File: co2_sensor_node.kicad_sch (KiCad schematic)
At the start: 6 parts, among them J1 Conn_01x05, J2 Conn_01x03

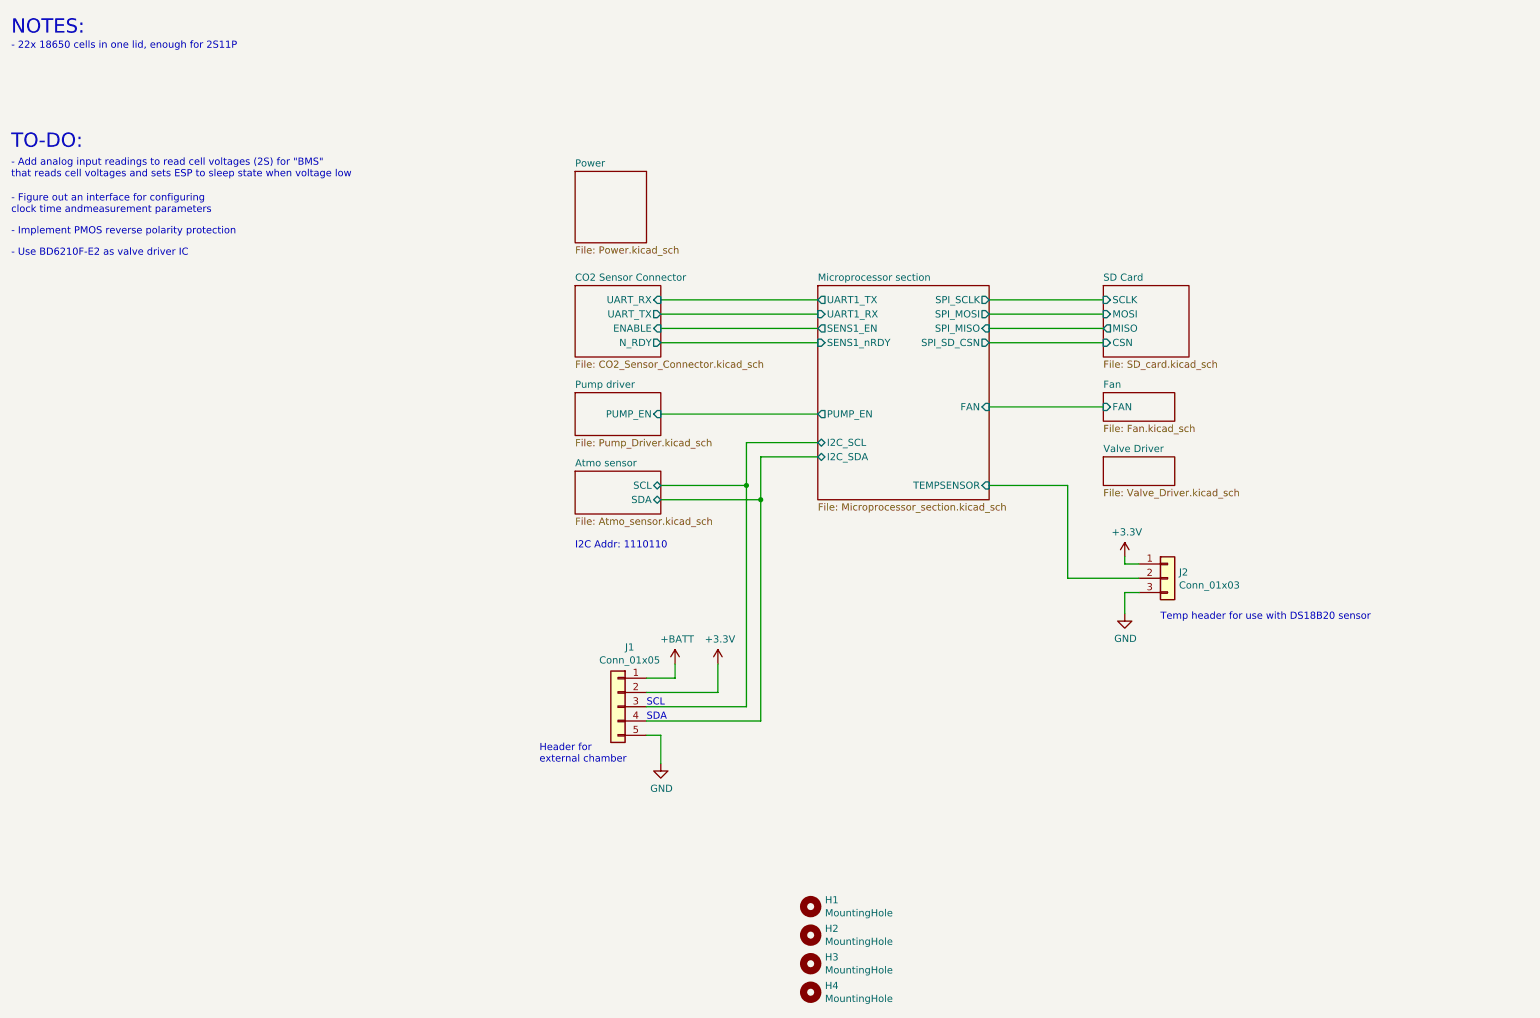
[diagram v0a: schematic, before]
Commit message: Move to KiCad v6, redesign circuit for chamber
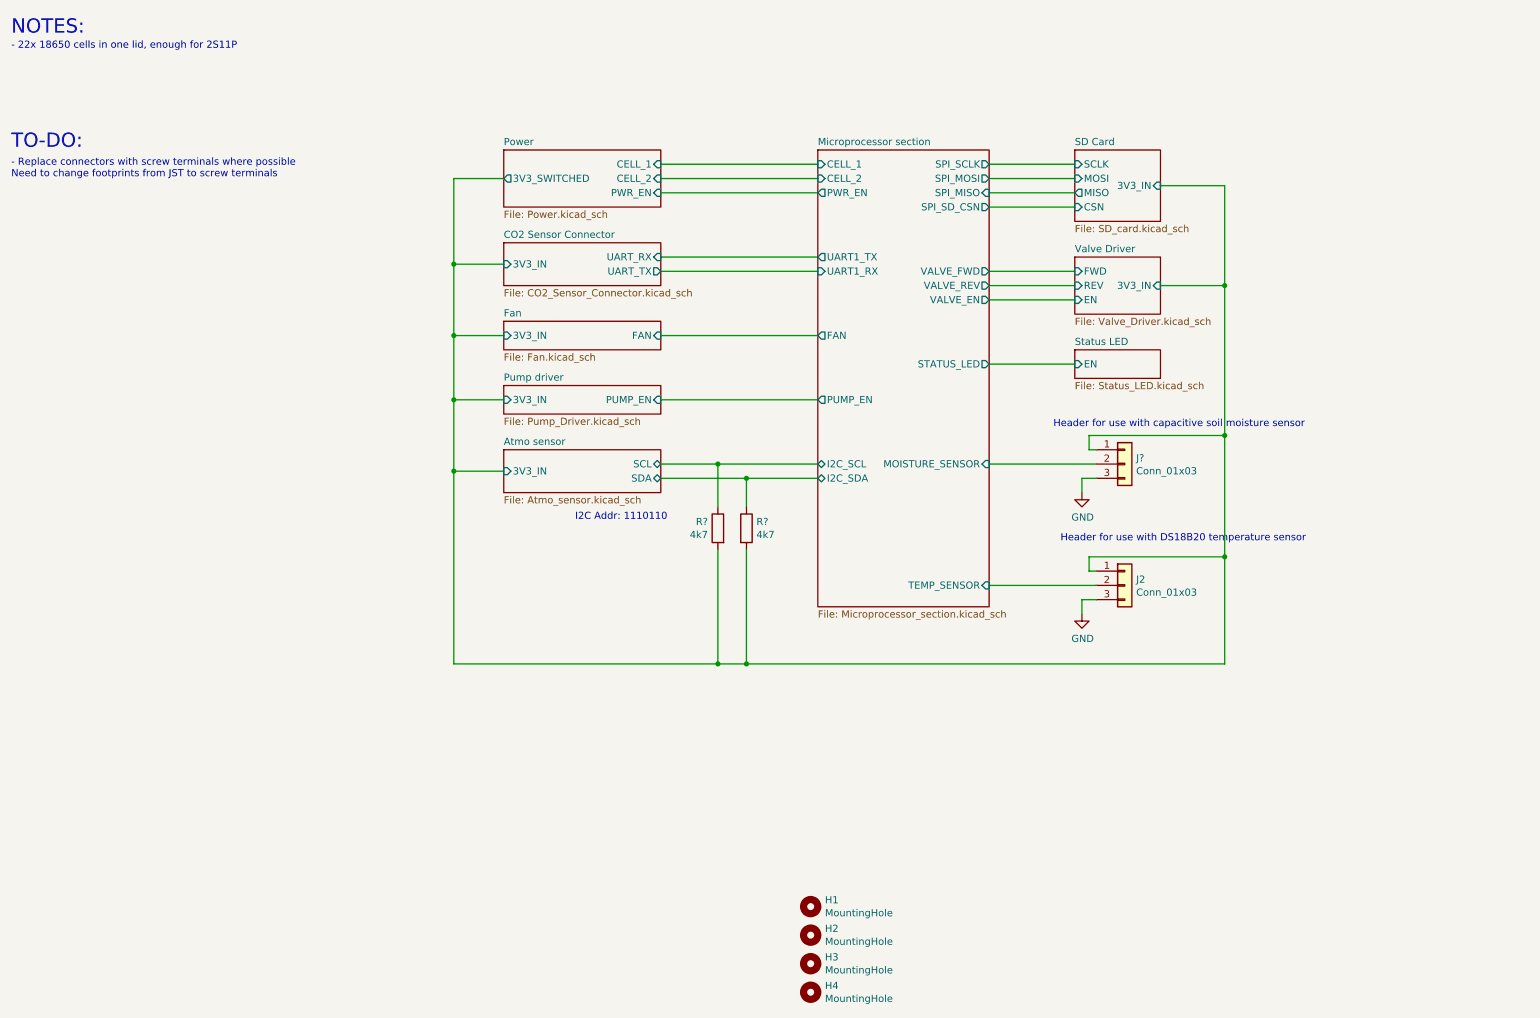
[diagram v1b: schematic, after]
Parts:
- removed J1: Conn_01x05, Connector_JST:JST_XH_B5B-XH-AM_1x05_P2.50mm_Vertical, symbol Connector_Generic:Conn_01x05
- added J?: Conn_01x03, Connector_JST:JST_XH_B3B-XH-AM_1x03_P2.50mm_Vertical, symbol Connector_Generic:Conn_01x03
- added R? (x2): 4k7, Resistor_SMD:R_0603_1608Metric, symbol Device:R
- J2: LCSC (none) -> C474882
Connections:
- net Atmo sensor/SCL: now also R?.1
- net Atmo sensor/SDA: now also R?.1
- net GND: now also J?.3 (Pin_3)
- net +3V3 renamed Atmo sensor/3V3_IN
- net Atmo sensor/3V3_IN: now also J?.1 (Pin_1), R?.2, R?.2
- net Microprocessor section/TEMPSENSOR renamed Microprocessor section/TEMP_SENSOR
- new net Microprocessor section/MOISTURE_SENSOR: J?.2 (Pin_2)
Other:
- added sheet Status LED (Status_LED.kicad_sch)
- sheet Atmo sensor ports: added 3V3_IN; removed none
- sheet CO2 Sensor Connector ports: added 3V3_IN; removed ENABLE, N_RDY
- sheet Fan ports: added 3V3_IN; removed none
- sheet Microprocessor section ports: added CELL_1, CELL_2, MOISTURE_SENSOR, PWR_EN, STATUS_LED, TEMP_SENSOR, VALVE_EN, VALVE_FWD, VALVE_REV; removed SENS1_EN, SENS1_nRDY, TEMPSENSOR
- sheet Power ports: added 3V3_SWITCHED, CELL_1, CELL_2, PWR_EN; removed none
- sheet Pump driver ports: added 3V3_IN; removed none
- sheet SD Card ports: added 3V3_IN; removed none
- sheet Valve Driver ports: added 3V3_IN, EN, FWD, REV; removed none
- note added: "- Replace connectors with screw terminals where possible Need to change footprints from JST to screw terminals"
- note added: "Header for use with DS18B20 temperature sensor"
- note added: "Header for use with capacitive soil moisture sensor"
- note removed: "- Add analog input readings to read cell voltages (2S) for "BMS" that reads cell voltages and sets ESP to sleep state when voltage low"
- note removed: "- Figure out an interface for configuring clock time andmeasurement parameters"
- note removed: "- Implement PMOS reverse polarity protection"
- note removed: "- Use BD6210F-E2 as valve driver IC"
- note removed: "Header for external chamber"
- note removed: "SCL"
- note removed: "SDA"
- note removed: "Temp header for use with DS18B20 sensor"
- moved on the sheet: J2

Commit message: Add test points, add JLC part numbers to JST XH connectors, clean up
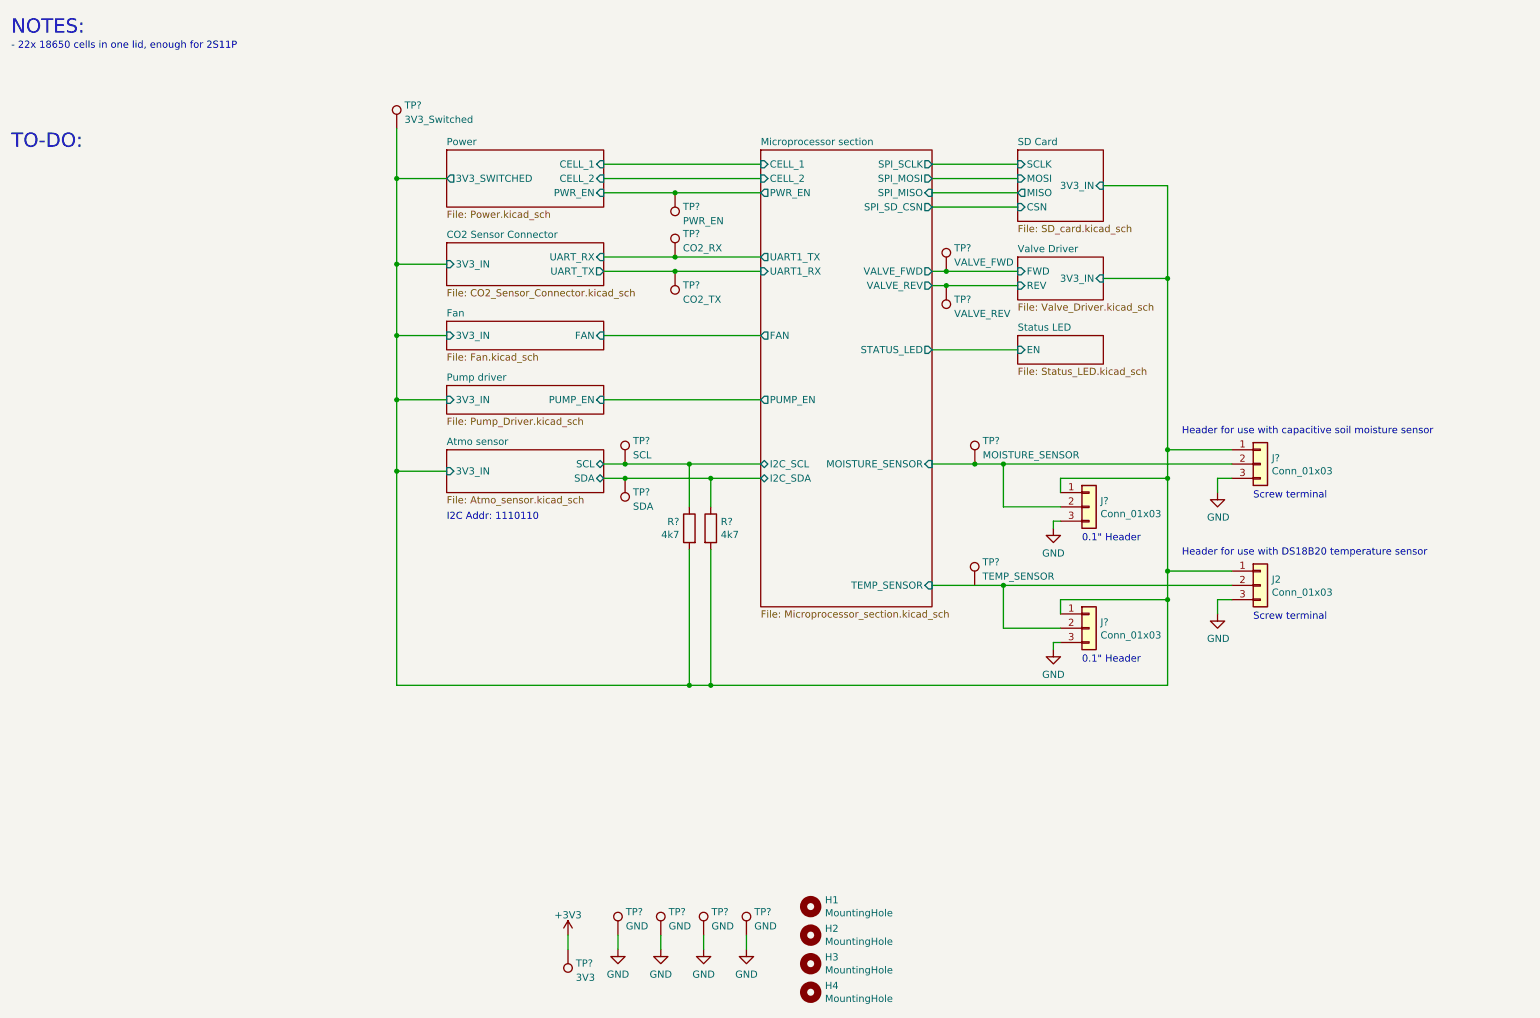
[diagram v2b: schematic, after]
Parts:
- added J? (x2): Conn_01x03, Connector_PinSocket_2.54mm:PinSocket_1x03_P2.54mm_Vertical, symbol Connector_Generic:Conn_01x03
- added TP?: SDA, symbol Connector:TestPoint
- added TP?: VALVE_REV, symbol Connector:TestPoint
- added TP?: SCL, symbol Connector:TestPoint
- added TP? (x4): GND, symbol Connector:TestPoint
- added TP?: PWR_EN, symbol Connector:TestPoint
- added TP?: VALVE_FWD, symbol Connector:TestPoint
- added TP?: 3V3_Switched, symbol Connector:TestPoint
- added TP?: CO2_RX, symbol Connector:TestPoint
- added TP?: TEMP_SENSOR, symbol Connector:TestPoint
- added TP?: MOISTURE_SENSOR, symbol Connector:TestPoint
- added TP?: 3V3, symbol Connector:TestPoint
- added TP?: CO2_TX, symbol Connector:TestPoint
- J2, J?: footprint Connector_JST:JST_XH_B3B-XH-AM_1x03_P2.50mm_Vertical -> co2_sensor_node:KF301-5.0-3P
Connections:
- net Atmo sensor/3V3_IN: now also J?.1 (Pin_1), J?.1 (Pin_1), TP?.1
- net Atmo sensor/SCL: now also TP?.1
- net Atmo sensor/SDA: now also TP?.1
- net CO2 Sensor Connector/UART_RX: now also TP?.1
- net CO2 Sensor Connector/UART_TX: now also TP?.1
- net GND: now also J?.3 (Pin_3), J?.3 (Pin_3), TP?.1, TP?.1, TP?.1, TP?.1
- net Microprocessor section/MOISTURE_SENSOR: now also J?.2 (Pin_2), TP?.1
- net Microprocessor section/PWR_EN: now also TP?.1
- net Microprocessor section/TEMP_SENSOR: now also J?.2 (Pin_2)
- net Microprocessor section/VALVE_FWD: now also TP?.1
- net Microprocessor section/VALVE_REV: now also TP?.1
- new net +3V3: TP?.1
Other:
- sheet Microprocessor section ports: added none; removed VALVE_EN
- sheet Valve Driver ports: added none; removed EN
- note added: "0.1" Header"
- note added: "Screw terminal"
- note removed: "- Replace connectors with screw terminals where possible Need to change footprints from JST to screw terminals"
- moved on the sheet: J2, J?, R?

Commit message: Add testpoint footprint assignments
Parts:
- TP1, TP10, TP11, TP12, TP13, TP14, TP15, TP2, TP3, TP4, TP5, TP6, TP7, TP8, TP9: renamed from TP?; footprint (none) -> TestPoint:TestPoint_Loop_D2.50mm_Drill1.0mm_LowProfile
- gave numbers to parts that had none: 5

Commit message: Finalize schematic
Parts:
- removed TP12: VALVE_FWD, TestPoint:TestPoint_Loop_D2.50mm_Drill1.0mm_LowProfile, symbol Connector:TestPoint
- removed TP13: VALVE_REV, TestPoint:TestPoint_Loop_D2.50mm_Drill1.0mm_LowProfile, symbol Connector:TestPoint
- added D1: Green LED, LED_SMD:LED_0603_1608Metric, symbol Device:LED
- added J3, J4: Conn_01x02, co2_sensor_node:KF301-5.0-2P, symbol Connector_Generic:Conn_01x02
- added R3: 1k, Resistor_SMD:R_0603_1608Metric, symbol Device:R
- renumbered J7 to J2, J8 to J5, J2 to J6, TP14 to TP12, TP15 to TP13, TP4 to TP2, TP5 to TP3, TP2 to TP4, TP7 to TP5, TP8 to TP6, TP9 to TP7, TP3 to TP8, TP6 to TP9
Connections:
- net GND: now also D1.1 (K)
- net Microprocessor section/STATUS_LED: now also R3.2
- new net: D1.2 (A), R3.1
- new net Valve Driver/OUT_A: J3.1 (Pin_1)
- new net Valve Driver/OUT_B: J3.2 (Pin_2)
- new net Valve Driver/OUT_C: J4.1 (Pin_1)
- new net Valve Driver/OUT_D: J4.2 (Pin_2)
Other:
- removed sheet Pump driver
- removed sheet Status LED
- sheet Microprocessor section ports: added VALVE_1_FWD, VALVE_1_REV, VALVE_2_FWD, VALVE_2_REV; removed PUMP_EN, VALVE_FWD, VALVE_REV
- sheet Valve Driver ports: added FWD_1, FWD_2, OUT_A, OUT_B, OUT_C, OUT_D, REV_1, REV_2; removed FWD, REV
- note added: "3V3"
- note added: "Valve 1 Screw terminal"
- note added: "Valve 2 Screw terminal"
- note removed: "- 22x 18650 cells in one lid, enough for 2S11P"
- note removed: "NOTES:"
- note removed: "TO-DO:"
- title: (none) -> CO2 Chamber - Top
- moved on the sheet: J1, J2, J5, J6, R1, R2, TP1, TP12, TP13, TP2, TP3, TP5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

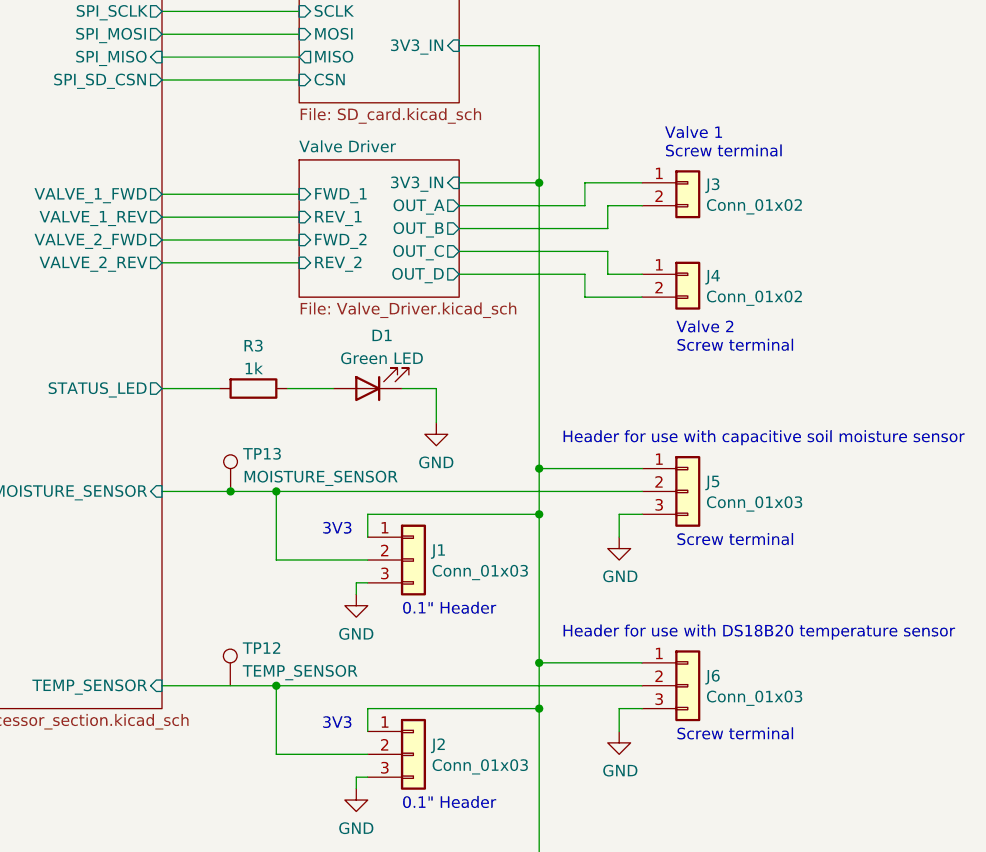
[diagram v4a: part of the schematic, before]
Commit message: Finish PCB layout
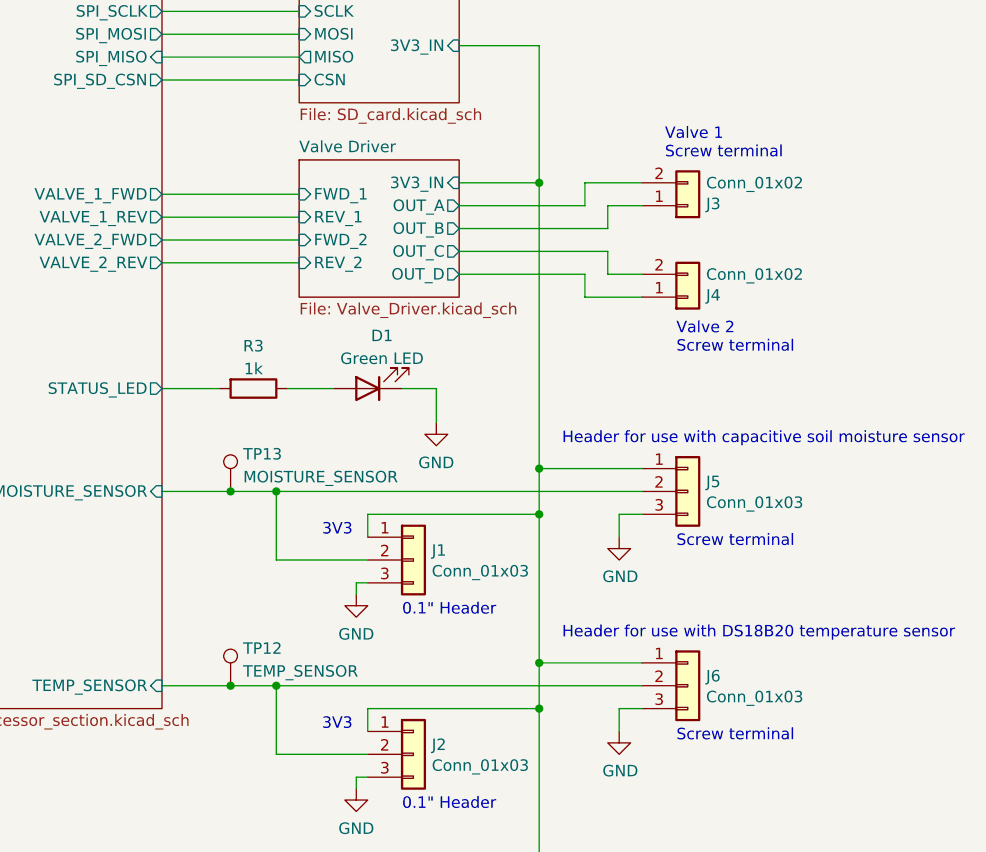
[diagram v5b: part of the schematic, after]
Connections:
- net Microprocessor section/TEMP_SENSOR: now also TP12.1
- net Valve Driver/OUT_A: now also J3.2 (Pin_2); no longer J3.1 (Pin_1)
- net Valve Driver/OUT_B: now also J3.1 (Pin_1); no longer J3.2 (Pin_2)
- net Valve Driver/OUT_C: now also J4.2 (Pin_2); no longer J4.1 (Pin_1)
- net Valve Driver/OUT_D: now also J4.1 (Pin_1); no longer J4.2 (Pin_2)
